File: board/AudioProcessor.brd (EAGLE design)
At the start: 49.5 x 45.7 mm, 47 parts, among them IC1 ATTINY24/44/84-SSU, IC2 LP2951, IC3 LP2951, IC4 TDA7439DS, J1 PINHD-1X3-JST-PH, J2 PINHD-1X3-JST-PH, J3 PINHD-1X3-JST-PH, J4 PINHD-1X3-JST-PH, J5 PINHD-1X3-JST-PH, J6 PINHD-1X6-JST-PH

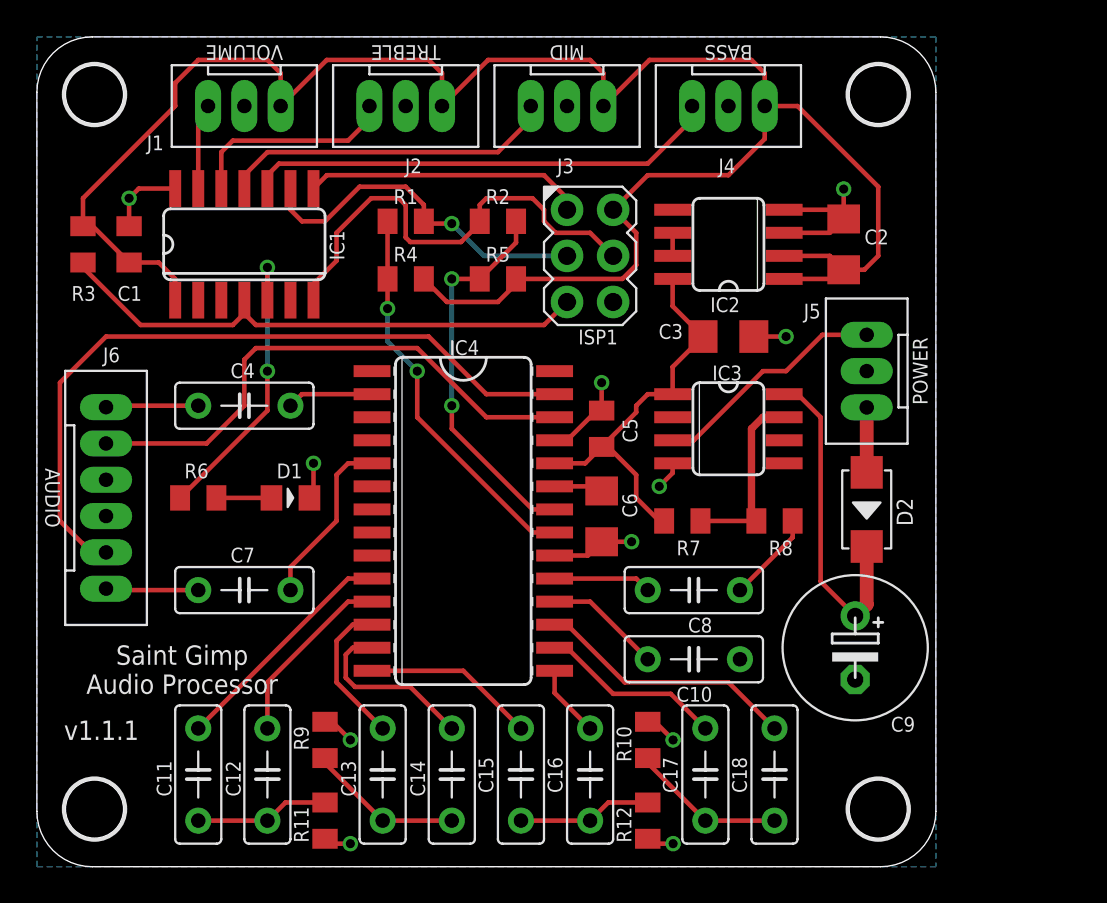
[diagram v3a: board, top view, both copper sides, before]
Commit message: Update with library changes and tune for Macrofab house parts
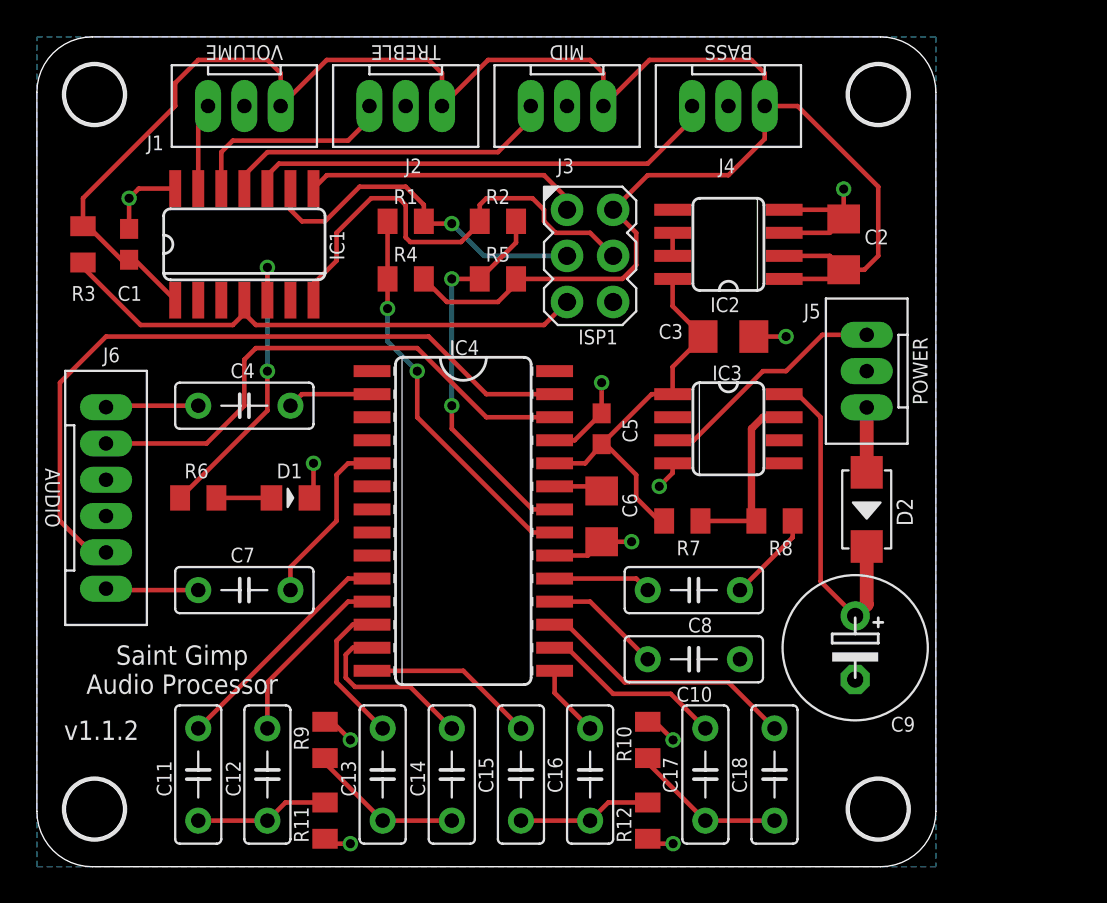
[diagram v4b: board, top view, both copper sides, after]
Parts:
- C1, C5: device SaintGimp:CAPACITOR-0805 -> SaintGimp:CAPACITOR-0603
- D2: value DIODE-DO214AC -> (none)
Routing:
- net +3V3: track 112.9 -> 112.3 mm
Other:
- board text added: "v1.1.2"
- board text removed: "v1.1.1"
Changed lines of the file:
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@@
 <text x="1.27" y="16.891" size="0.8128" layer="122" rot="SMR90" align="top-center">LOUT</text>
 <text x="1.27" y="13.716" size="0.8128" layer="122" rot="SMR90" align="top-center">LIN</text>
-<text x="3.556" y="6.985" size="1.0668" layer="121" rot="R180" align="top-center">v1.1.1</text>
+<text x="3.556" y="6.985" size="1.0668" layer="121" rot="R180" align="top-center">v1.1.2</text>
 </plain>
 <attributes>
@@
 <attribute name="NAME" x="45.593" y="34.29" size="0.8128" layer="25"/>
 </element>
-<element name="C5" library="SaintGimp" package="CAPACITOR-0805" value="0.1uF" x="31.115" y="24.13" smashed="yes" rot="R90">
+<element name="C5" library="SaintGimp" package="CAPACITOR-0603" value="0.1uF" x="31.115" y="24.13" smashed="yes" rot="R90">
 <attribute name="NAME" x="33.0835" y="23.368" size="0.8128" layer="25" rot="R90"/>
 </element>
-<element name="C1" library="SaintGimp" package="CAPACITOR-0805" value="0.1uF" x="5.08" y="34.29" smashed="yes" rot="R270">
+<element name="C1" library="SaintGimp" package="CAPACITOR-0603" value="0.1uF" x="5.08" y="34.29" smashed="yes" rot="R270">
 <attribute name="NAME" x="4.445" y="31.1785" size="0.8128" layer="25"/>
 </element>
@@
 </element>
 <element name="D1" library="SaintGimp" package="LED-0805" value="LED-0805" x="13.97" y="20.32"/>
-<element name="D2" library="SaintGimp" package="DO-214AC" value="DIODE-DO214AC" x="45.72" y="19.685" smashed="yes" rot="R270">
+<element name="D2" library="SaintGimp" package="DO-214AC" value="" x="45.72" y="19.685" smashed="yes" rot="R270">
 <attribute name="NAME" x="47.371" y="20.32" size="0.889" layer="25" ratio="11" rot="R270"/>
 </element>
@@
 <via x="31.115" y="26.67" extent="1-16" drill="0.5"/>
 <via x="32.766" y="17.907" extent="1-16" drill="0.5"/>
-<wire x1="31.115" y1="26.67" x2="31.115" y2="25.13" width="0.254" layer="1"/>
+<wire x1="31.115" y1="26.67" x2="31.115" y2="24.98" width="0.254" layer="1"/>
 <via x="17.272" y="1.27" extent="1-16" drill="0.5"/>
 <wire x1="17.272" y1="1.27" x2="16.145" y2="1.27" width="0.254" layer="1"/>
@@
 <via x="5.08" y="36.83" extent="1-16" drill="0.5"/>
 <wire x1="44.45" y1="36.195" x2="44.45" y2="37.338" width="0.254" layer="1"/>
-<wire x1="5.08" y1="35.29" x2="5.08" y2="36.83" width="0.254" layer="1"/>
+<wire x1="5.08" y1="35.14" x2="5.08" y2="36.83" width="0.254" layer="1"/>
 <wire x1="7.62" y1="37.3634" x2="5.6134" y2="37.3634" width="0.254" layer="1"/>
 <wire x1="5.6134" y1="37.3634" x2="5.08" y2="36.83" width="0.254" layer="1"/>
@@
 <wire x1="33.925" y1="1.27" x2="33.655" y2="1.54" width="0.254" layer="1"/>
 <contactref element="C9" pad="-"/>
-<wire x1="31.115" y1="25.13" x2="30.845" y2="25.13" width="0.254" layer="1"/>
-<wire x1="29.21" y1="23.495" x2="28.5242" y2="23.495" width="0.254" layer="1"/>
-<wire x1="30.845" y1="25.13" x2="29.21" y2="23.495" width="0.254" layer="1"/>
 <wire x1="28.5242" y1="17.145" x2="30.356" y2="17.145" width="0.254" layer="1"/>
 <wire x1="30.356" y1="17.145" x2="31.115" y2="17.904" width="0.254" layer="1"/>
@@
 <wire x1="38.735" y1="15.24" x2="41.64" y2="18.145" width="0.254" layer="1"/>
 <wire x1="41.64" y1="18.145" x2="41.64" y2="19.05" width="0.254" layer="1"/>
+<wire x1="31.115" y1="24.98" x2="29.63" y2="23.495" width="0.254" layer="1"/>
+<wire x1="29.63" y1="23.495" x2="28.5242" y2="23.495" width="0.254" layer="1"/>
 </signal>
 <signal name="N$3">
@@
 <contactref element="C3" pad="1"/>
 <contactref element="IC2" pad="8"/>
-<wire x1="31.115" y1="23.13" x2="30.21" y2="22.225" width="0.254" layer="1"/>
+<wire x1="31.115" y1="23.28" x2="30.21" y2="22.225" width="0.254" layer="1"/>
 <wire x1="30.21" y1="22.225" x2="28.5242" y2="22.225" width="0.254" layer="1"/>
-<wire x1="35.0266" y1="26.035" x2="33.655" y2="26.035" width="0.254" layer="1"/>
-<wire x1="33.655" y1="26.035" x2="33.02" y2="25.4" width="0.254" layer="1"/>
-<wire x1="33.02" y1="25.4" x2="33.02" y2="25.035" width="0.254" layer="1"/>
-<wire x1="33.02" y1="25.035" x2="31.115" y2="23.13" width="0.254" layer="1"/>
 <wire x1="34.56" y1="19.05" x2="34.29" y2="19.05" width="0.254" layer="1"/>
 <wire x1="34.29" y1="19.05" x2="33.02" y2="20.32" width="0.254" layer="1"/>
 <wire x1="33.02" y1="20.32" x2="33.02" y2="21.59" width="0.254" layer="1"/>
 <wire x1="33.02" y1="21.59" x2="31.48" y2="23.13" width="0.254" layer="1"/>
-<wire x1="31.48" y1="23.13" x2="31.115" y2="23.13" width="0.254" layer="1"/>
+<wire x1="31.48" y1="23.13" x2="31.115" y2="23.28" width="0.254" layer="1"/>
 <wire x1="35.0266" y1="32.385" x2="35.0266" y2="30.8834" width="0.254" layer="1"/>
 <wire x1="35.0266" y1="30.8834" x2="36.7" y2="29.21" width="0.254" layer="1"/>
 <wire x1="36.7" y1="29.21" x2="35.0266" y2="27.5366" width="0.254" layer="1"/>
 <wire x1="35.0266" y1="27.5366" x2="35.0266" y2="26.035" width="0.254" layer="1"/>
+<wire x1="35.0266" y1="26.035" x2="33.87" y2="26.035" width="0.254" layer="1"/>
+<wire x1="33.87" y1="26.035" x2="31.115" y2="23.28" width="0.254" layer="1"/>
 </signal>
 <signal name="L-OUT">
@@
 <contactref element="J4" pad="1"/>
 <wire x1="44.45" y1="32.385" x2="44.45" y2="32.89" width="0.254" layer="1"/>
-<wire x1="5.08" y1="33.29" x2="6.715" y2="33.29" width="0.254" layer="1"/>
-<wire x1="6.715" y1="33.29" x2="7.62" y2="32.385" width="0.254" layer="1"/>
-<wire x1="7.62" y1="32.385" x2="7.62" y2="31.2166" width="0.254" layer="1"/>
 <wire x1="33.02" y1="34.925" x2="31.75" y2="36.195" width="0.254" layer="1"/>
 <wire x1="33.02" y1="34.925" x2="33.02" y2="33.147" width="0.254" layer="1"/>
@@
 <wire x1="45.59" y1="32.89" x2="46.355" y2="33.655" width="0.254" layer="1"/>
 <wire x1="46.355" y1="33.655" x2="46.355" y2="37.465" width="0.254" layer="1"/>
-<wire x1="2.54" y1="35.29" x2="3.08" y2="35.29" width="0.254" layer="1"/>
-<wire x1="3.08" y1="35.29" x2="5.08" y2="33.29" width="0.254" layer="1"/>
 <wire x1="33.655" y1="38.1" x2="38.1" y2="38.1" width="0.254" layer="1"/>
 <wire x1="38.1" y1="38.1" x2="40.1" y2="40.1" width="0.254" layer="1"/>
@@
 <wire x1="7.62" y1="43.18" x2="7.62" y2="41.91" width="0.254" layer="1"/>
 <wire x1="7.62" y1="41.91" x2="2.54" y2="36.83" width="0.254" layer="1"/>
-<wire x1="2.54" y1="36.83" x2="2.54" y2="35.29" width="0.254" layer="1"/>
+<wire x1="2.54" y1="35.56" x2="2.54" y2="36.83" width="0.254" layer="1"/>
+<wire x1="2.54" y1="35.56" x2="2.54" y2="35.29" width="0.254" layer="1"/>
+<wire x1="4.66" y1="33.44" x2="5.08" y2="33.44" width="0.254" layer="1"/>
+<wire x1="4.66" y1="33.44" x2="2.54" y2="35.56" width="0.254" layer="1"/>
+<wire x1="5.08" y1="33.44" x2="5.3966" y2="33.44" width="0.254" layer="1"/>
+<wire x1="5.3966" y1="33.44" x2="7.62" y2="31.2166" width="0.254" layer="1"/>
 </signal>
 <signal name="L-IN">
